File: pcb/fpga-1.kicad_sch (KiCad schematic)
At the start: 3 parts

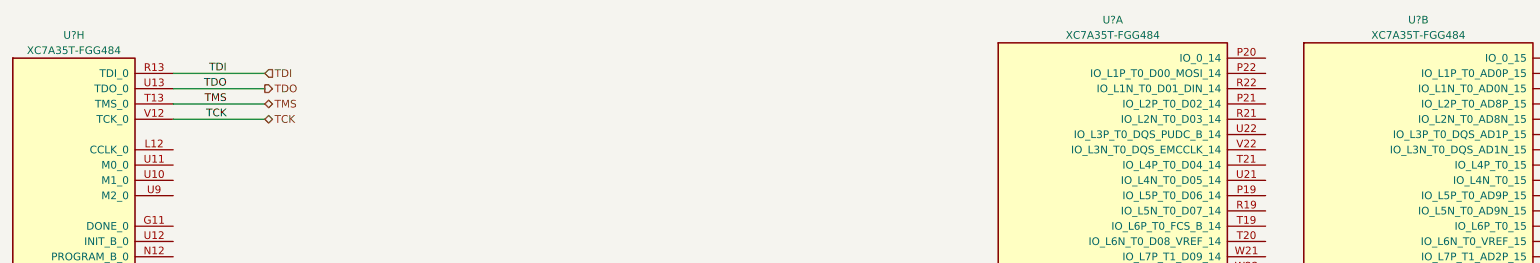
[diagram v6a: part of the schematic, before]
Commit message: completed bus aliasing definitions
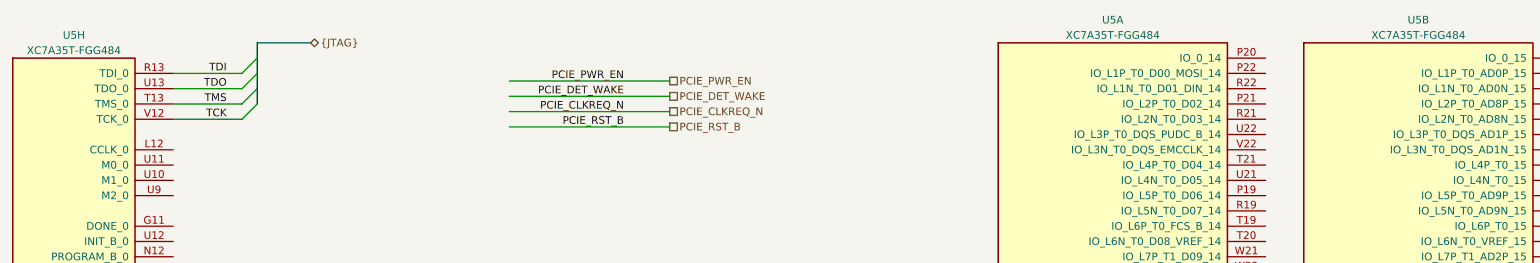
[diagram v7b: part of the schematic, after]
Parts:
- gave numbers to parts that had none: 1
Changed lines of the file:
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@@
 		(company "Andre S Winkel")
 	)
+	(bus_entry
+		(at 59.69 34.29)
+		(size 2.54 -2.54)
+		(stroke
+			(width 0)
+			(type default)
+		)
+	)
+	(bus_entry
+		(at 59.69 29.21)
+		(size 2.54 -2.54)
+		(stroke
+			(width 0)
+			(type default)
+		)
+	)
+	(bus_entry
+		(at 59.69 26.67)
+		(size 2.54 -2.54)
+		(stroke
+			(width 0)
+			(type default)
+		)
+	)
+	(bus_entry
+		(at 59.69 31.75)
+		(size 2.54 -2.54)
+		(stroke
+			(width 0)
+			(type default)
+		)
+	)
+	(wire
+		(pts
+			(xy 48.26 26.67) (xy 59.69 26.67)
+		)
+		(stroke
+			(width 0)
+			(type default)
+		)
+	)
+	(wire
+		(pts
+			(xy 104.14 35.56) (xy 130.81 35.56)
+		)
+		(stroke
+			(width 0)
+			(type default)
+		)
+	)
+	(bus
+		(pts
+			(xy 62.23 31.75) (xy 62.23 29.21)
+		)
+		(stroke
+			(width 0)
+			(type default)
+		)
+	)
 	(wire
 		(pts
-			(xy 48.26 26.67) (xy 63.5 26.67)
+			(xy 48.26 29.21) (xy 59.69 29.21)
 		)
 		(stroke
@@
 	(wire
 		(pts
-			(xy 48.26 29.21) (xy 63.5 29.21)
+			(xy 104.14 27.94) (xy 130.81 27.94)
 		)
 		(stroke
@@
 	(wire
 		(pts
-			(xy 48.26 31.75) (xy 63.5 31.75)
+			(xy 104.14 30.48) (xy 130.81 30.48)
+		)
+		(stroke
+			(width 0)
+			(type default)
+		)
+	)
+	(bus
+		(pts
+			(xy 62.23 26.67) (xy 62.23 24.13)
 		)
 		(stroke
@@
 	(wire
 		(pts
-			(xy 48.26 34.29) (xy 63.5 34.29)
+			(xy 104.14 33.02) (xy 130.81 33.02)
+		)
+		(stroke
+			(width 0)
+			(type default)
+		)
+	)
+	(bus
+		(pts
+			(xy 62.23 21.59) (xy 71.12 21.59)
+		)
+		(stroke
+			(width 0)
+			(type default)
+		)
+	)
+	(wire
+		(pts
+			(xy 48.26 31.75) (xy 59.69 31.75)
+		)
+		(stroke
+			(width 0)
+			(type default)
+		)
+	)
+	(bus
+		(pts
+			(xy 62.23 29.21) (xy 62.23 26.67)
+		)
+		(stroke
+			(width 0)
+			(type default)
+		)
+	)
+	(wire
+		(pts
+			(xy 48.26 34.29) (xy 59.69 34.29)
+		)
+		(stroke
+			(width 0)
+			(type default)
+		)
+	)
+	(bus
+		(pts
+			(xy 62.23 24.13) (xy 62.23 21.59)
 		)
 		(stroke
@@
 		)
 	)
+	(label "PCIE_DET_WAKE"
+		(at 123.19 30.48 180)
+		(effects
+			(font
+				(size 1.27 1.27)
+			)
+			(justify right bottom)
+		)
+	)
 	(label "TMS"
 		(at 57.15 31.75 180)
@@
 		)
 	)
+	(label "PCIE_CLKREQ_N"
+		(at 123.19 33.02 180)
+		(effects
+			(font
+				(size 1.27 1.27)
+			)
+			(justify right bottom)
+		)
+	)
 	(label "TDI"
 		(at 57.15 26.67 180)
@@
 		)
 	)
-	(hierarchical_label "TDI"
-		(shape input)
-		(at 63.5 26.67 0)
+	(label "PCIE_RST_B"
+		(at 123.19 35.56 180)
+		(effects
+			(font
+				(size 1.27 1.27)
+			)
+			(justify right bottom)
+		)
+	)
+	(label "PCIE_PWR_EN"
+		(at 123.19 27.94 180)
+		(effects
+			(font
+				(size 1.27 1.27)
+			)
+			(justify right bottom)
+		)
+	)
+	(hierarchical_label "PCIE_DET_WAKE"
+		(shape passive)
+		(at 130.81 30.48 0)
 		(effects
 			(font
@@
 		)
 	)
-	(hierarchical_label "TDO"
-		(shape output)
-		(at 63.5 29.21 0)
+	(hierarchical_label "PCIE_RST_B"
+		(shape passive)
+		(at 130.81 35.56 0)
 		(effects
 			(font
@@
 		)
 	)
-	(hierarchical_label "TCK"
-		(shape bidirectional)
-		(at 63.5 34.29 0)
+	(hierarchical_label "PCIE_PWR_EN"
+		(shape passive)
+		(at 130.81 27.94 0)
+		(effects
+			(font
+				(size 1.27 1.27)
+			)
+			(justify left)
+		)
+	)
+	(hierarchical_label "PCIE_CLKREQ_N"
+		(shape passive)
+		(at 130.81 33.02 0)
 		(effects
 			(font
@@
 		)
 	)
-	(hierarchical_label "TMS"
+	(hierarchical_label "{JTAG}"
 		(shape bidirectional)
-		(at 63.5 31.75 0)
+		(at 71.12 21.59 0)
 		(effects
 			(font
 				(size 1.27 1.27)
+				(thickness 0.1588)
 			)
 			(justify left)
@@
 		(dnp no)
 		(fields_autoplaced yes)
-		(property "Reference" "U?"
+		(property "Reference" "U5"
 			(at 255.27 17.78 0)
 			(effects
@@
 			(project "RPi-HwAB-1"
 				(path "/e63e39d7-6ac0-4ffd-8aa3-1841a4541b55/59d21473-a004-4514-8090-fd93db818925/350bfe7d-9948-4ca7-a542-a75eb385def4"
-					(reference "U?")
+					(reference "U5")
 					(unit 2)
 				)
@@
 		(dnp no)
 		(fields_autoplaced yes)
-		(property "Reference" "U?"
+		(property "Reference" "U5"
 			(at 204.47 17.78 0)
 			(effects
@@
 			(project "RPi-HwAB-1"
 				(path "/e63e39d7-6ac0-4ffd-8aa3-1841a4541b55/59d21473-a004-4514-8090-fd93db818925/350bfe7d-9948-4ca7-a542-a75eb385def4"
-					(reference "U?")
+					(reference "U5")
 					(unit 1)
 				)
@@
 		(dnp no)
 		(fields_autoplaced yes)
-		(property "Reference" "U?"
+		(property "Reference" "U5"
 			(at 31.75 20.32 0)
 			(effects
@@
 			(project "RPi-HwAB-1"
 				(path "/e63e39d7-6ac0-4ffd-8aa3-1841a4541b55/59d21473-a004-4514-8090-fd93db818925/350bfe7d-9948-4ca7-a542-a75eb385def4"
-					(reference "U?")
+					(reference "U5")
 					(unit 8)
 				)
